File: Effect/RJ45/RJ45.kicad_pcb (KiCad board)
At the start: 2 copper layers, 30 x 84 mm, 6 parts, among them J1 Conn_01x04_Pin, J2 RJ45, J3 Conn_01x03_Pin

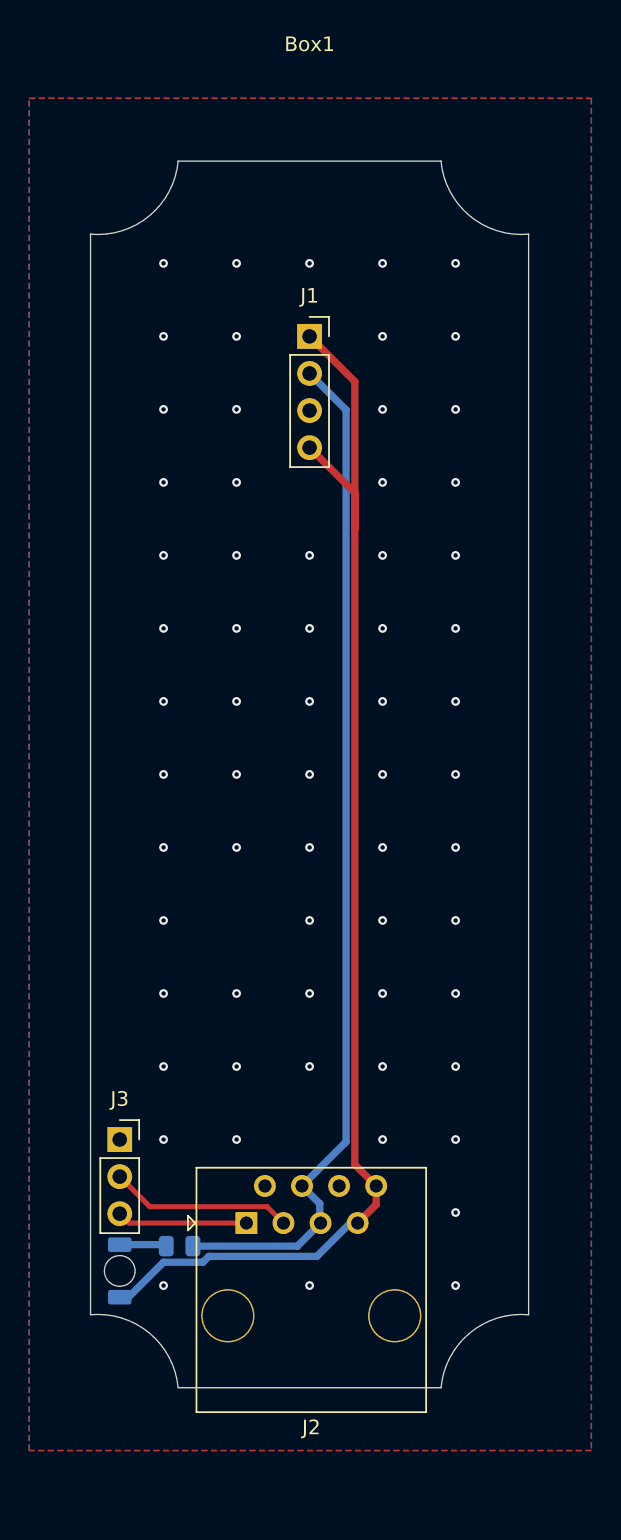
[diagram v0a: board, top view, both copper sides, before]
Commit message: Switch to a shielded RJ45 connector for the RJ45 test boards
It turns out that all my ethernet cables I had around look to be plain
unshielded twisted pairs (UTP), and some very preliminary testing shows
that they are very noisy and I'd need to use differential signalling to
make the whole "connect the base and effect with an ethernet cable"
scheme work.

I know, I know, that's technically the right thing to do anyway, but I
really don't think it's an option.  It adds way too much effort at the
effects end, at that point I'm better off just keeping the two together.

Even if some of my recent circuits have been differential (ie that whole
multiplier thing), I don't want to force that on everything.

And yes, the ethernet cable idea might have been a stupid idea and any
first-year EE would probably have told me that.  I'm a SW guy, remember?

But before giving up, let's just try the single-ended model with proper
shielded cables and shielded connectors.  The double-shielded cables are
a thing, with each twisted pair foil-shielded and then the whole cable
having a braided shield.

That would seem to be no worse than a normal 1/4" audio cable, even if
the same cable also carries power.  I'm looking for a few feet, not long
runs.  Knock wood.

And the shielding is part of the CAT8 specs, so this is standard cable
these days and cheap, even if my random box of cables was full of the
old crappy stuff of yesteryear.

So maybe this model is still salvageable with single-ended signaling.
Because I'd love to separate the stomp switch and audio jacks from the
actual effect side.

Signed-off-by: Linus Torvalds <torvalds@linux-foundation.org>
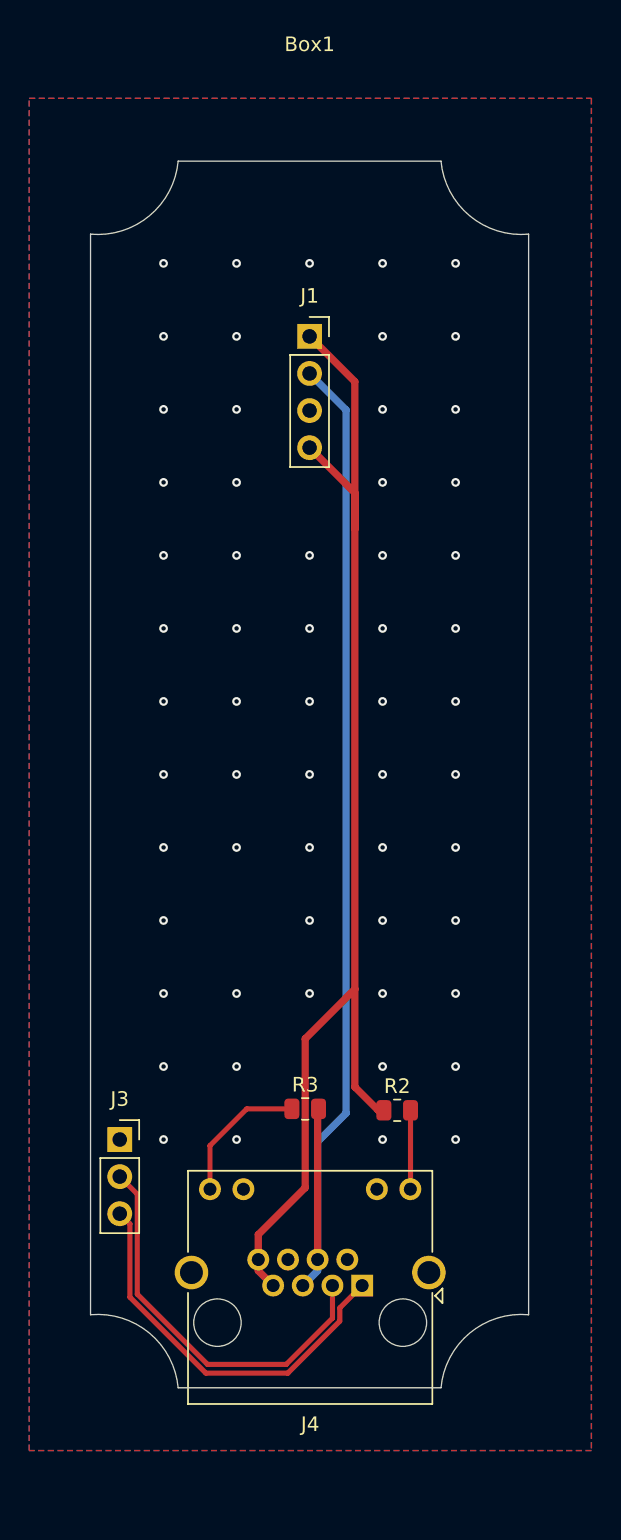
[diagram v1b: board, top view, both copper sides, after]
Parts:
- removed D1: LED, Mylib:Würth Reverse Mount LED
- removed J2: RJ45, Connector_RJ:RJ45_OST_PJ012-8P8CX_Vertical
- removed R1: 10k, Resistor_SMD:R_0805_2012Metric
- added J4: RJ45_LED_Shielded, Connector_RJ:RJ45_Amphenol_RJHSE538X, F.Cu at (103.6, 135.0)
- added R2: 2.2k, Resistor_SMD:R_0805_2012Metric, F.Cu at (106.0, 123.0)
- added R3: 2.2k, Resistor_SMD:R_0805_2012Metric, F.Cu at (99.7, 122.9)
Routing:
- net IN: track 8.94 -> 27.1 mm
- net OUT: track 12.5 -> 27.5 mm
- net Net-(J4-Pad12): track 0.00 -> 9.63 mm
- net Net-(J4-Pad9): track 0.00 -> 5.41 mm
- net +V: track 70.3 -> 75.1 mm
- net Net-(D1-A): track 3.09 -> 0.00 mm
- net -V: track 88.4 -> 85.7 mm
- net GND: vias 64 -> 59

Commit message: RJ45: update the "effect conversion" board to be active
... and hopefully make it work right.

The old hacky one was truly just a hack, and was a passive feed-through
of the signals from the RJ45 jack to the old effect board pin headers.

That was hacky mainly because it ignored the whole new world order wrt
voltages (ie the RJ45 cable carries dual voltage rails, the old effect
boards expect the VGND thing).

But it was also hacky because it expected the effects board to just deal
with the fact that the output now went to that RJ45 jack - and that
obviously didn't work very well for the base board, so why would it work
for the effects boards?

So this redoes the conversion board to actually buffer and rebias the
signals, and it basically looks a lot like the old VGND board except it
doesn't have a stomp switch or audio jacks, because all of that is
obviously on the new RJ45 base board.

I put all the components on the front, which in hindsight might have
been a mistake: it means that the joiner and splitter boards won't work
because they won't physically fit any more.  But if we want those in the
new RJ45 regime, I think they probably make more sense as actual new
boards anyway.

Will this work out ok? I still have no idea.  But nothing for it but
try.

Signed-off-by: Linus Torvalds <torvalds@linux-foundation.org>
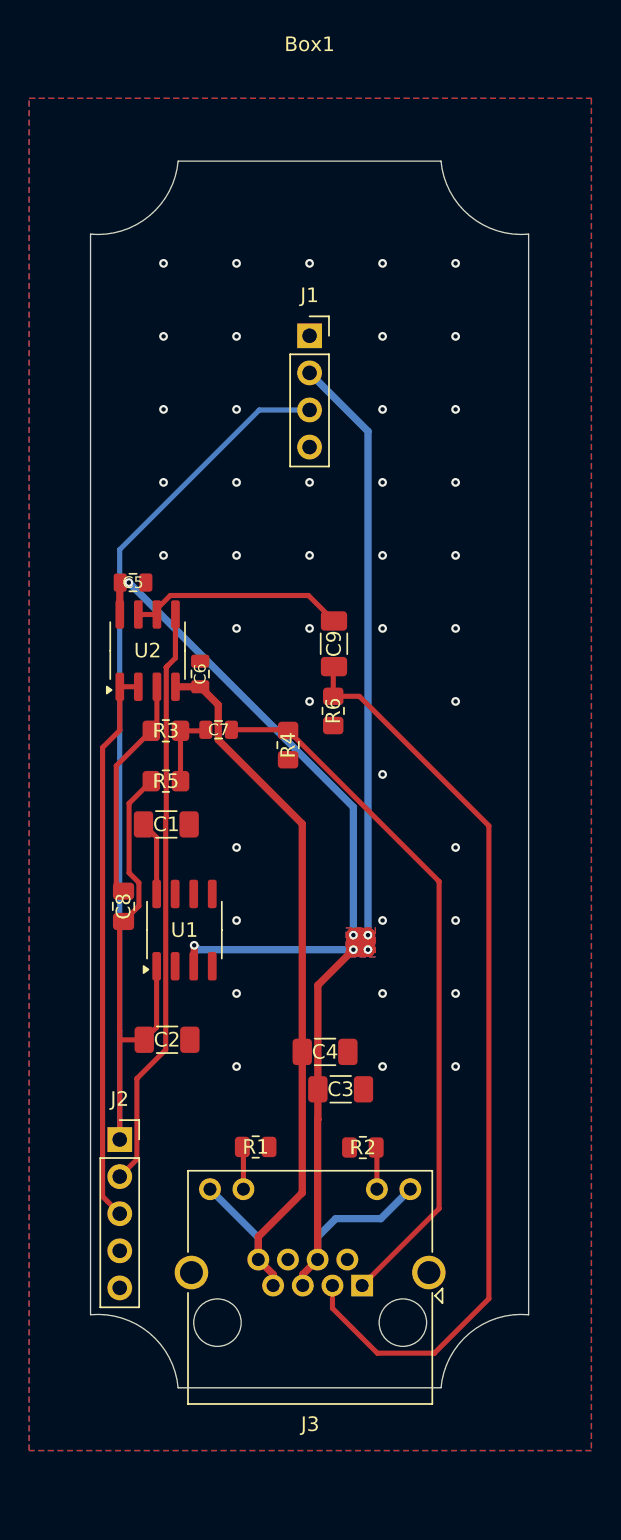
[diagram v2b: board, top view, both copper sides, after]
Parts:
- removed the J3 at (87.0, 125.0)
- added C1: 1uF, Capacitor_SMD:C_1206_3216Metric_Pad1.33x1.80mm_HandSolder, F.Cu at (90.2, 103.4)
- added C2: 10uF, Capacitor_SMD:C_1206_3216Metric_Pad1.33x1.80mm_HandSolder, F.Cu at (90.2, 118.2)
- added C3: 22uF, Capacitor_SMD:C_1206_3216Metric_Pad1.33x1.80mm_HandSolder, F.Cu at (102.1, 121.6)
- added C4: 22uF, Capacitor_SMD:C_1206_3216Metric_Pad1.33x1.80mm_HandSolder, F.Cu at (101.1, 119.0)
- added C5: 0.1uF, Mylib:C_0704_1810Metric, F.Cu at (87.9, 86.9)
- added C6: 0.1uF, Mylib:C_0704_1810Metric, F.Cu at (92.5, 93.1)
- added C7: 0.1uF, Mylib:C_0704_1810Metric, F.Cu at (93.8, 96.9)
- added C8: 220pF, Capacitor_SMD:C_0805_2012Metric_Pad1.18x1.45mm_HandSolder, F.Cu at (87.3, 109.0)
- added C9: 0.47uF, Capacitor_SMD:C_1206_3216Metric_Pad1.33x1.80mm_HandSolder, F.Cu at (101.7, 91.0)
- added J2: Conn_01x05_Pin, Connector_PinSocket_2.54mm:PinSocket_1x05_P2.54mm_Vertical, F.Cu at (87.0, 125.0)
- added R3: 1k, Resistor_SMD:R_0805_2012Metric_Pad1.20x1.40mm_HandSolder, F.Cu at (90.2, 97.0)
- added R4: 1M0, Resistor_SMD:R_0805_2012Metric_Pad1.20x1.40mm_HandSolder, F.Cu at (98.5, 98.0)
- added R5: 470k, Resistor_SMD:R_0805_2012Metric_Pad1.20x1.40mm_HandSolder, F.Cu at (90.2, 100.5)
- added R6: 100k, Resistor_SMD:R_0805_2012Metric_Pad1.20x1.40mm_HandSolder, F.Cu at (101.6, 95.7)
- added U1: TLE2426xD, Package_SO:SOIC-8_3.9x4.9mm_P1.27mm, F.Cu at (91.4, 110.7)
- added U2: OPA1656, Package_SO:SOIC-8_3.9x4.9mm_P1.27mm, F.Cu at (88.9, 91.5)
- moved R1 4.28 mm to (96.3, 125.5)
- moved R2 3.47 mm to (103.7, 125.5), turned to 180 degrees
- renumbered J4 to J3, R3 to R1
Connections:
- J1 pad 1: -V -> GND
- J1 pad 3: GND -> GNDREF
- J1 pad 4: -V -> GND
- J3 pad 1: IN -> IN^{RAW}
- J3 pad 10: GND -> Net-(J3-Pad10)
- J3 pad 11: GND -> Net-(J3-Pad11)
- J3 pad 12: Net-(J4-Pad12) -> -V
- J3 pad 3: OUT -> OUT^{RAW}
- J3 pad 9: Net-(J4-Pad9) -> +V
- R1 pad 1: Net-(J4-Pad12) -> Net-(J3-Pad11)
- R1 pad 2: +V -> GND
- R2 pad 1: -V -> Net-(J3-Pad10)
- R2 pad 2: Net-(J4-Pad9) -> GND
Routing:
- net GNDREF: track 0.00 -> 90.0 mm
- net OUT^{RAW}: track 0.00 -> 63.8 mm
- net +V: track 75.1 -> 123.7 mm, vias 0 -> 6
- net IN^{RAW}: track 0.00 -> 48.3 mm
- net OUT^{EFF}: track 0.00 -> 40.2 mm
- net IN^{EFF}: track 0.00 -> 38.3 mm
- net -V: track 85.7 -> 53.5 mm
- net OUT: track 27.5 -> 0.00 mm
- net IN: track 27.1 -> 0.00 mm
- net Net-(U2A-+): track 0.00 -> 14.8 mm
- net Net-(U2B--): track 0.00 -> 14.5 mm
- net Net-(J4-Pad12): track 9.63 -> 0.00 mm
- net Net-(J4-Pad9): track 5.41 -> 0.00 mm
- net Net-(U1-NOISE_REDUCTION): track 0.00 -> 5.14 mm
- net Net-(C7-Pad2): track 0.00 -> 5.11 mm
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- added copper zone on B.Cu, net +V
- added copper zone on F.Cu, net +V

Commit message: Update the RJ45 boards
So I'm doing two different cable versions in parallel to see which I
like better.  The "passive base board" version uses USB-C connectors and
really doesn't do anything at all but convert the power, stomp switch
and audio connectors to one single cable.  So the effects board is
supposed to do everything that is actually signal-related, including
generating its own reference voltages etc.

In contrast, the RJ45 board is "active", and also generates a negative
power rail.  That doesn't help the existing effects boards, but it means
that any boards actively designed for this have all the voltages
(assuming +-9V and GND works for them), and don't need to rebias signals
etc.

Do I know which board - if any - I'm actually going to develop further?
No.  They may both be garbage.

Signed-off-by: Linus Torvalds <torvalds@linux-foundation.org>
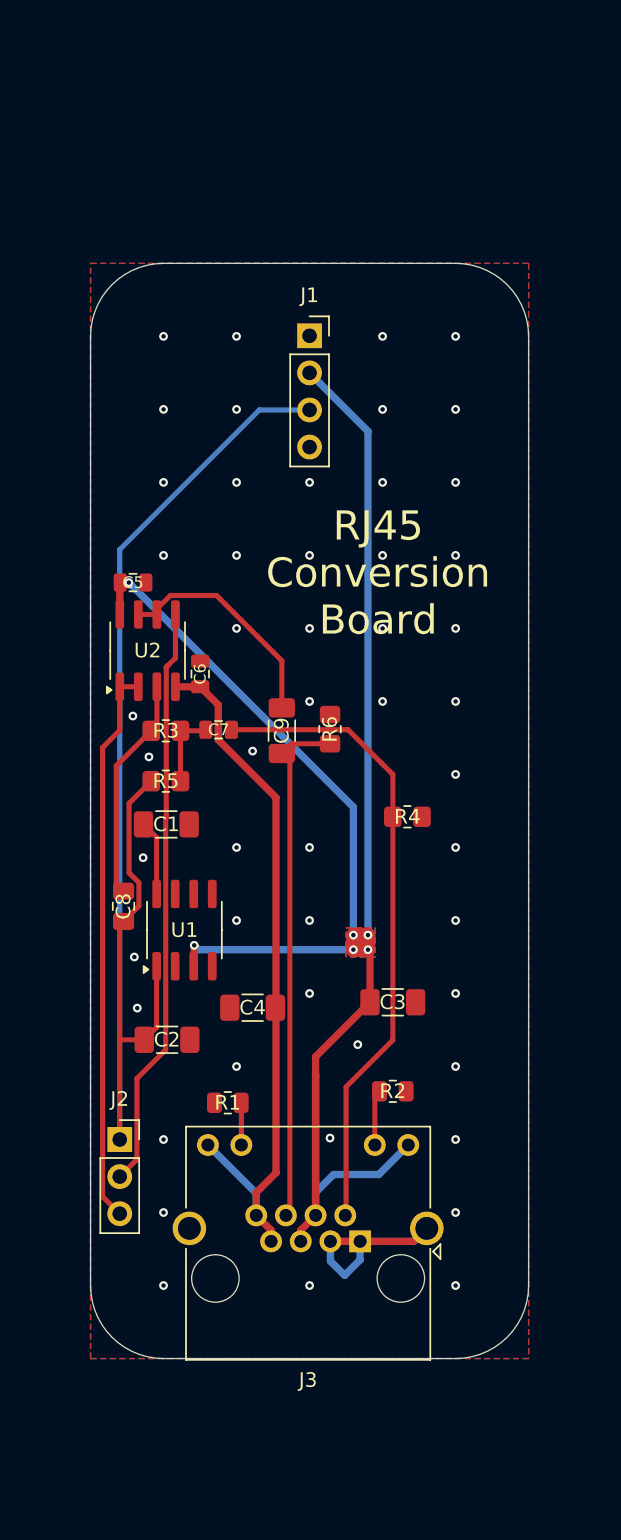
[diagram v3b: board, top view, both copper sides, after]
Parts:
- removed Box1: 1590A, Mylib:1590A
- J2: value Conn_01x05_Pin -> Conn_01x03_Pin; footprint Connector_PinSocket_2.54mm:PinSocket_1x05_P2.54mm_Vertical -> Connector_PinSocket_2.54mm:PinSocket_1x03_P2.54mm_Vertical
- moved R4 9.53 mm to (106.7, 102.9), turned to 0 degrees
- moved C3 6.95 mm to (105.7, 115.6)
- moved C9 6.94 mm to (98.1, 97.0)
- moved C4 5.81 mm to (96.1, 116.0), turned to 180 degrees
- moved R2 4.36 mm to (105.7, 121.7), turned to 0 degrees
- moved R1 3.58 mm to (94.4, 122.5), turned to 180 degrees
- moved J3 3.03 mm to (103.5, 132.0)
- moved R6 1.27 mm to (101.4, 96.9), turned to 90 degrees
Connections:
- J3 pad 1: IN^{RAW} -> GND
- J3 pad 2: GND -> IN^{RAW}
- J3 pad 3: OUT^{RAW} -> GND
- J3 pad 6: GND -> OUT^{RAW}
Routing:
- net OUT^{RAW}: track 63.8 -> 35.5 mm
- net GND: track 0.00 -> 19.4 mm, vias 41 -> 51
- net +V: track 123.7 -> 130.8 mm
- net -V: track 53.5 -> 49.0 mm
- net IN^{RAW}: track 48.3 -> 43.9 mm
- net Net-(J3-Pad10): track 2.80 -> 3.81 mm
- net Net-(U2B--): track 14.5 -> 15.3 mm
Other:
- board size 30 x 84 mm -> 30 x 75 mm
- board text added: "RJ45 Conversion Board"
